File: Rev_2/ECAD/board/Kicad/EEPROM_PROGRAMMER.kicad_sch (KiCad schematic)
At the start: 4 parts, among them U1 FT232RL

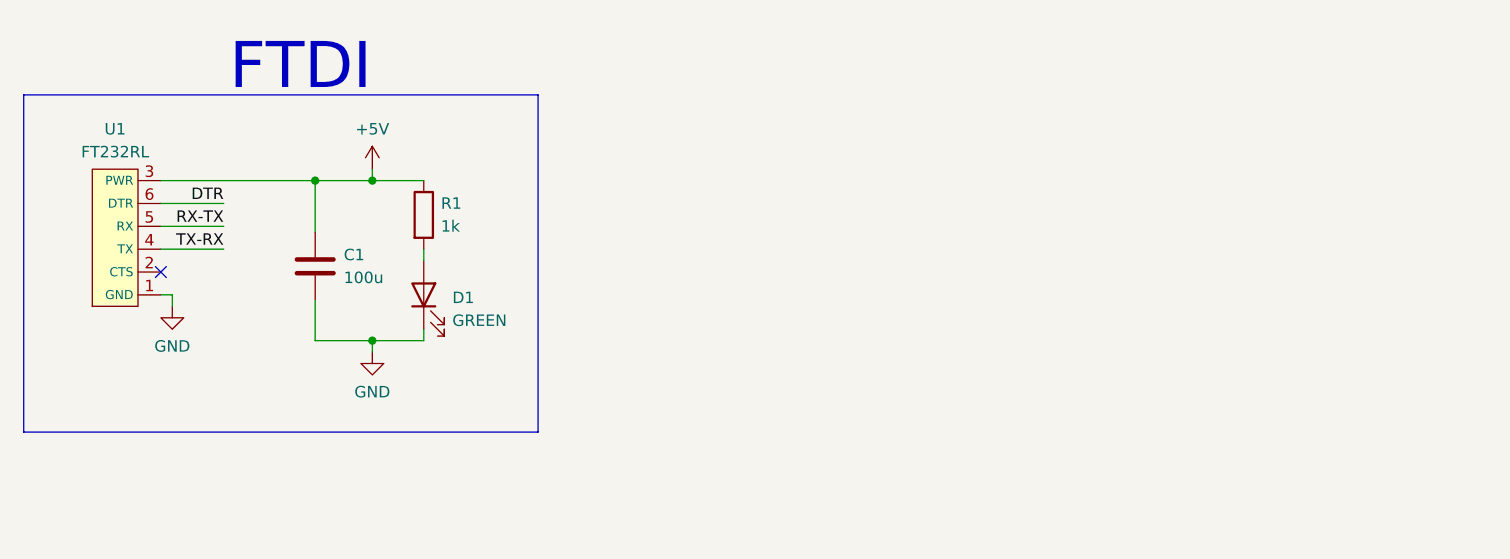
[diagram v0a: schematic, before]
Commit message: Added Reverse Polarity Protection and Overvoltage Portection
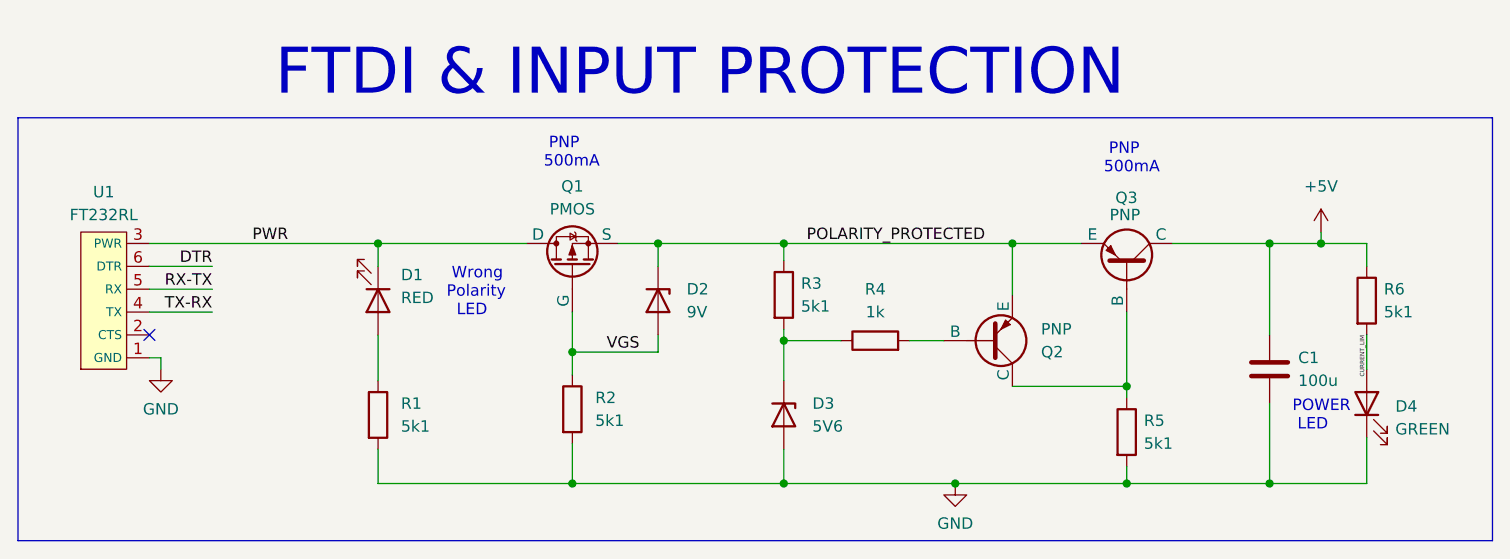
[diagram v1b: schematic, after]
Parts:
- added D1: RED, LED_SMD:LED_0805_2012Metric_Pad1.15x1.40mm_HandSolder, symbol Device:LED
- added D2: 9V, symbol Device:D_Zener
- added D3: 5V6, symbol Device:D_Zener
- added Q1: PMOS, Package_TO_SOT_SMD:SOT-23, symbol Simulation_SPICE:PMOS
- added Q2: PNP, Package_TO_SOT_SMD:SOT-23, symbol Simulation_SPICE:PNP
- added Q3: PNP, Package_TO_SOT_THT:TO-92, symbol Simulation_SPICE:PNP
- added R1, R2, R3, R5: 5k1, Resistor_SMD:R_0805_2012Metric_Pad1.20x1.40mm_HandSolder, symbol Device:R
- added R4: 1k, Resistor_SMD:R_0805_2012Metric_Pad1.20x1.40mm_HandSolder, symbol Device:R
- C1: footprint (none) -> Capacitor_THT:CP_Radial_D6.3mm_P2.50mm
- R6: renamed from R1; value 1k -> 5k1
- renumbered D1 to D4
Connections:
- net +5V: now also Q3.1 (C); no longer U1.3 (PWR)
- net GND: now also D3.2 (A), R1.2, R2.2, R5.2
- net CURRENT_LIM: now reaches D4.2 (A), R6.2
- new net: D3.1 (K), R3.2, R4.1
- new net: Q2.2 (B), R4.2
- new net: Q2.1 (C), Q3.2 (B), R5.1
- new net: D1.2 (A), R1.1
- new net POLARITY_PROTECTED: D2.1 (K), Q1.3 (S), Q2.3 (E), Q3.3 (E), R3.1
- new net PWR: D1.1 (K), Q1.1 (D), U1.3 (PWR)
- new net VGS: D2.2 (A), Q1.2 (G), R2.1
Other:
- note added: "FTDI & INPUT PROTECTION"
- note added: "PNP 500mA"
- note added: "POWER LED"
- note added: "Wrong Polarity LED"
- note removed: "FTDI"
- moved on the sheet: C1, D4, R6, U1

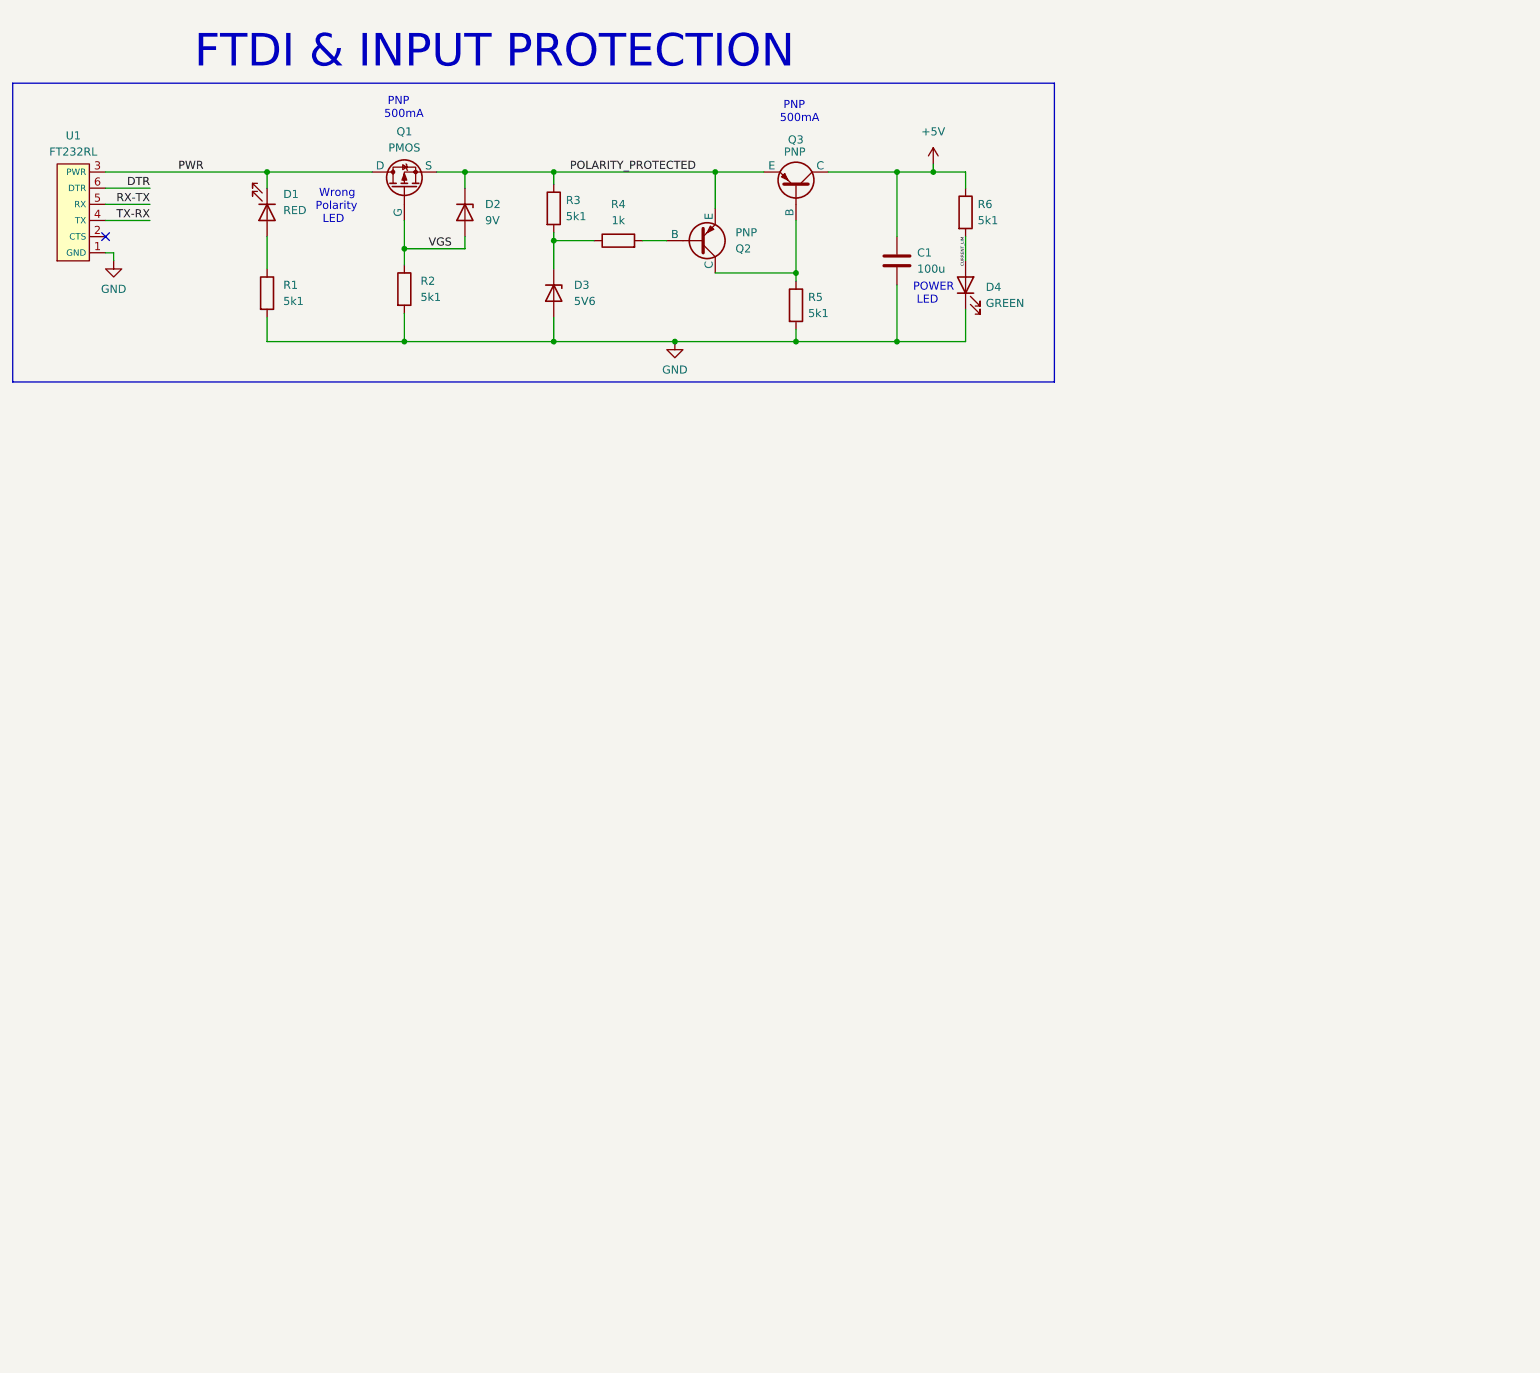
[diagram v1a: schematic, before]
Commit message: Added Atmega328 to the schematic
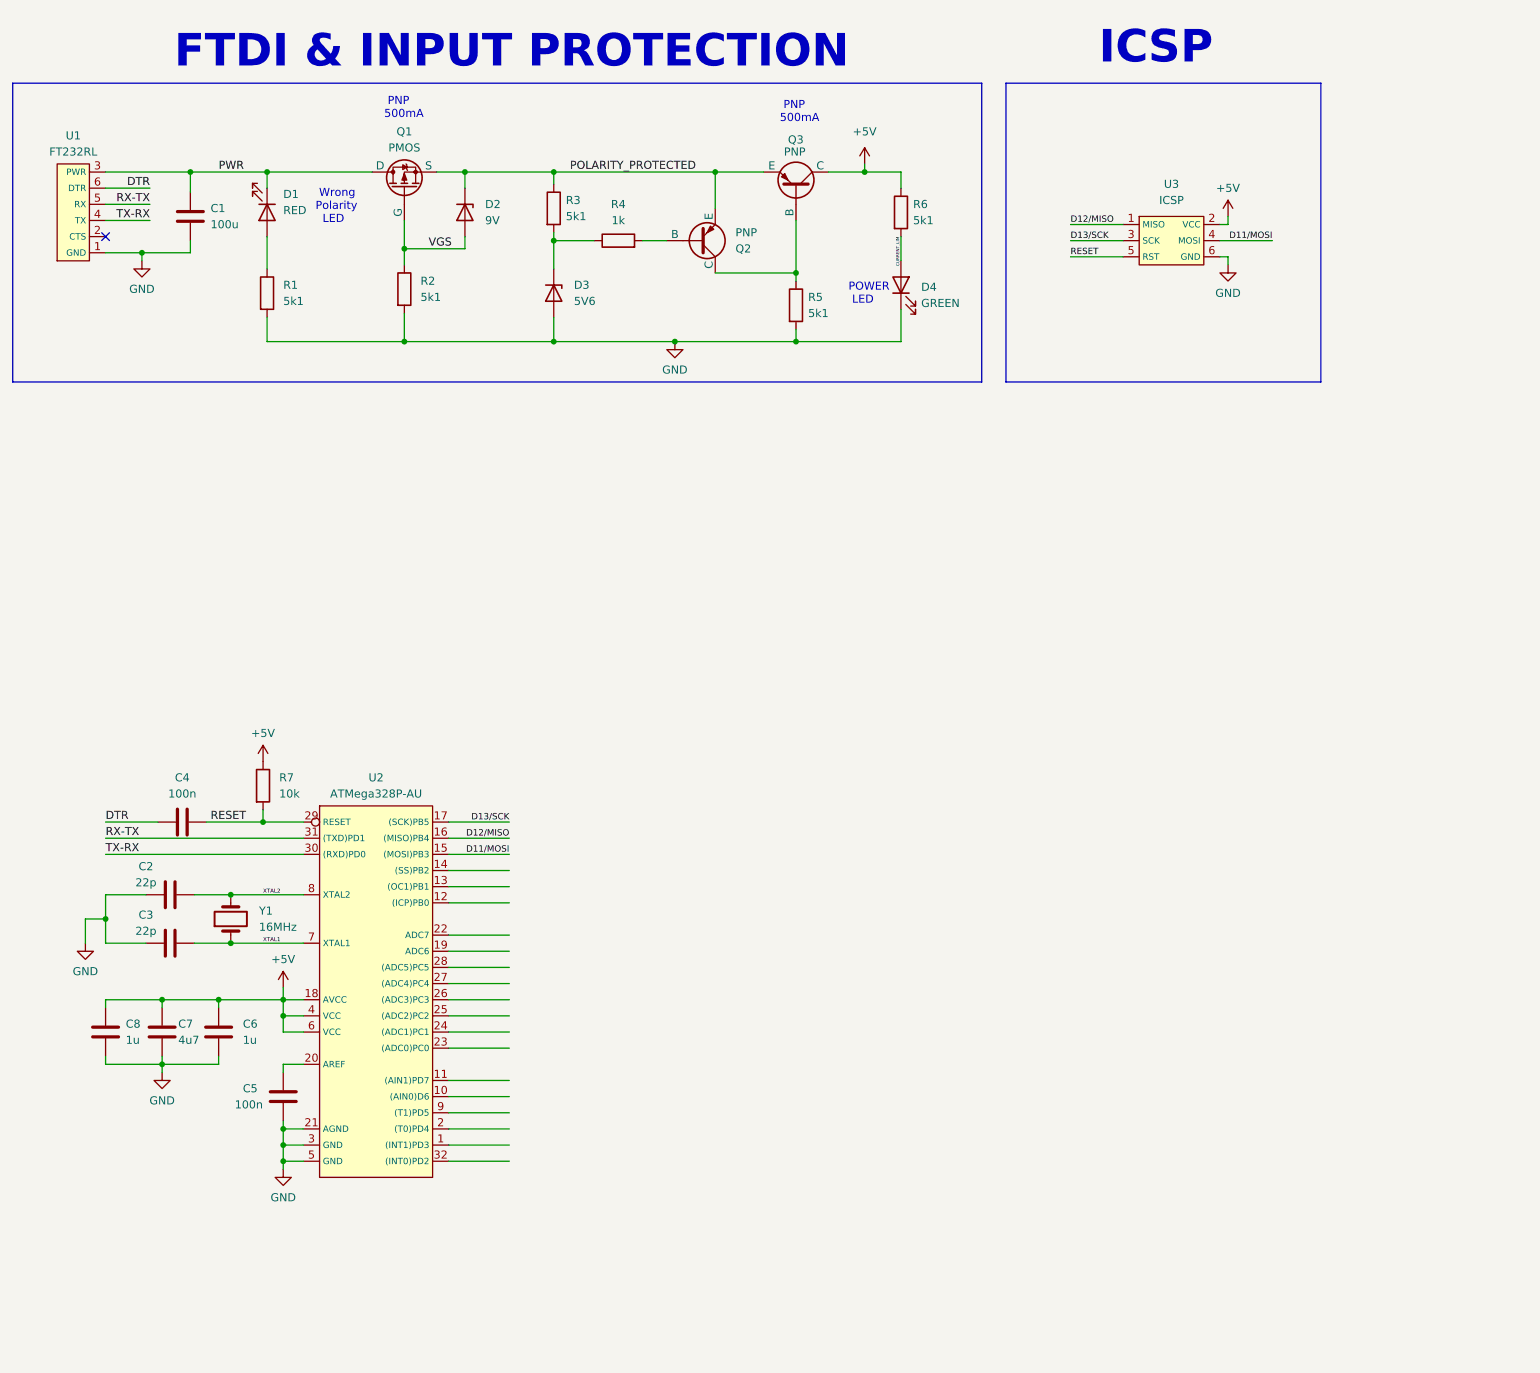
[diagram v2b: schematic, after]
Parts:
- added C2, C3: 22p, Capacitor_THT:CP_Radial_D6.3mm_P2.50mm, symbol Device:C
- added C4, C5: 100n, Capacitor_THT:CP_Radial_D6.3mm_P2.50mm, symbol Device:C
- added C6, C8: 1u, Capacitor_THT:CP_Radial_D6.3mm_P2.50mm, symbol Device:C
- added C7: 4u7, Capacitor_THT:CP_Radial_D6.3mm_P2.50mm, symbol Device:C
- added R7: 10k, Resistor_SMD:R_0805_2012Metric_Pad1.20x1.40mm_HandSolder, symbol Device:R
- added U2: ATMega328P-AU, EEPROM_PROGRAMMER:ATMega328P-AU, symbol EEPROM_PROGRAMMER:ATMega328P-AU
- added U3: ICSP, EEPROM_PROGRAMMER:ICSP, symbol EEPROM_PROGRAMMER:ICSP
- added Y1: 16MHz, symbol Device:Crystal
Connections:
- net +5V: now also C6.2, C7.2, C8.2, R7.1, U2.18 (AVCC), U2.4 (VCC), U2.6 (VCC), U3.2 (VCC); no longer C1.1
- net DTR: now also C4.1
- net GND: now also C2.1, C3.1, C5.1, C6.1, C7.1, C8.1, U2.21 (AGND), U2.3 (GND), U2.5 (GND), U3.6 (GND)
- net PWR: now also C1.1
- net RX-TX: now also U2.31 ((TXD)PD1)
- net TX-RX: now also U2.30 ((RXD)PD0)
- new net: C5.2, U2.20 (AREF)
- new net D11/MOSI: U2.15 ((MOSI)PB3), U3.4 (MOSI)
- new net D12/MISO: U2.16 ((MISO)PB4), U3.1 (MISO)
- new net D13/SCK: U2.17 ((SCK)PB5), U3.3 (SCK)
- new net RESET: C4.2, R7.2, U2.29 (RESET), U3.5 (RST)
- new net XTAL1: C3.2, U2.7 (XTAL1), Y1.1
- new net XTAL2: C2.2, U2.8 (XTAL2), Y1.2
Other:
- note added: "ICSP"
- moved on the sheet: D4, R6

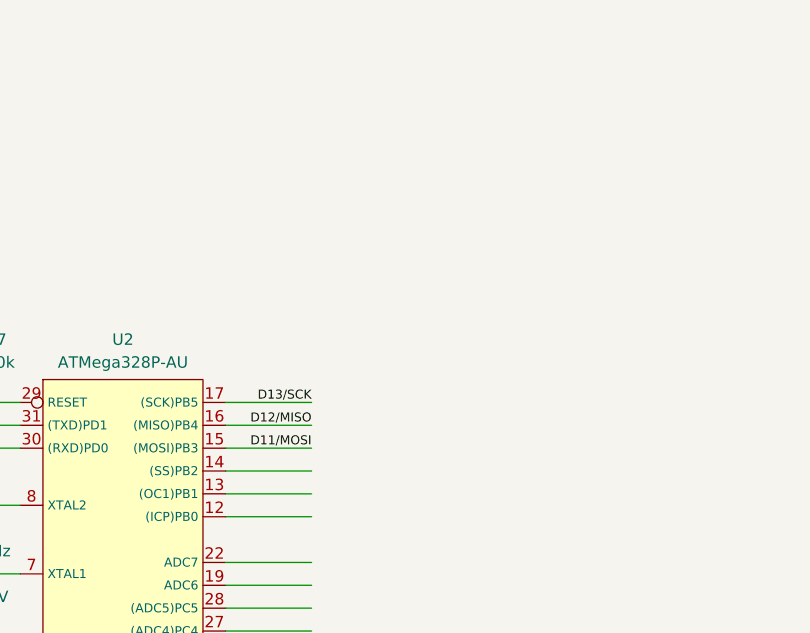
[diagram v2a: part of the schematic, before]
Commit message: Added SD-Card Reader to schematic
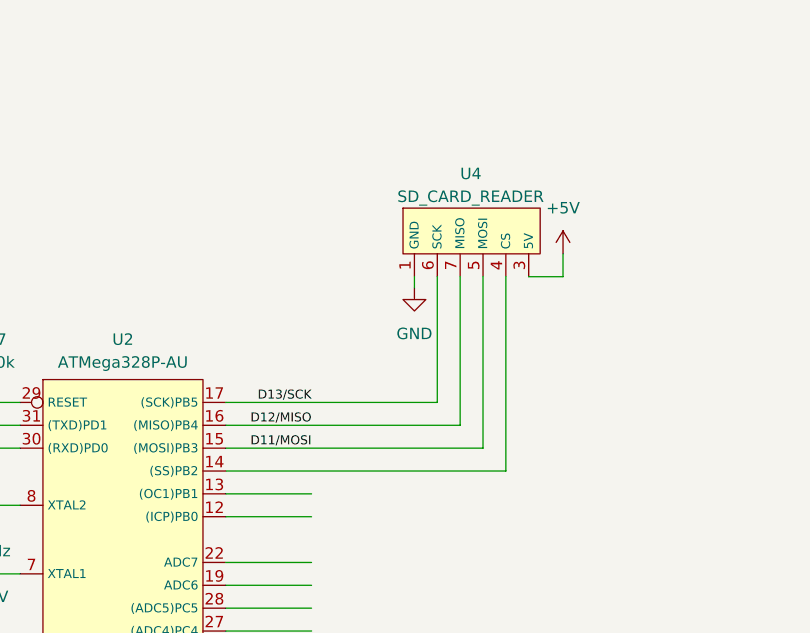
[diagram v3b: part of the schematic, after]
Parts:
- added U4: SD_CARD_READER, EEPROM_PROGRAMMER:SD_CARD_READER, symbol EEPROM_PROGRAMMER:SD_CARD_READER
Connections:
- net +5V: now also U4.3 (5V)
- net D11/MOSI: now also U4.5 (MOSI)
- net D12/MISO: now also U4.7 (MISO)
- net D13/SCK: now also U4.6 (SCK)
- net GND: now also U4.1 (GND)
- net at U2.14 ((SS)PB2): now also U4.4 (CS)
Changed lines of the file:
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@@
-    (stroke (width 0) (type default))
-  )
-  (wire (pts (xy 85.725 146.05) (xy 95.25 146.05))
     (stroke (width 0) (type default))
   )
@@
     (stroke (width 0) (type default))
   )
+  (wire (pts (xy 109.22 127) (xy 109.22 140.97))
+    (stroke (width 0) (type default))
+  )
   (wire (pts (xy 62.865 189.23) (xy 59.69 189.23))
     (stroke (width 0) (type default))
@@
     (stroke (width 0) (type default))
   )
+  (wire (pts (xy 116.84 127) (xy 116.84 148.59))
+    (stroke (width 0) (type default))
+  )
   (wire (pts (xy 140.335 65.405) (xy 156.845 65.405))
     (stroke (width 0) (type default))
@@
     (stroke (width 0) (type default))
   )
+  (wire (pts (xy 111.76 127) (xy 111.76 143.51))
+    (stroke (width 0) (type default))
+  )
   (wire (pts (xy 102.235 40.64) (xy 102.235 38.735))
     (stroke (width 0) (type default))
   )
+  (wire (pts (xy 85.725 146.05) (xy 114.3 146.05))
+    (stroke (width 0) (type default))
+  )
   (wire (pts (xy 208.28 45.72) (xy 208.28 46.99))
     (stroke (width 0) (type default))
@@
     (stroke (width 0) (type default))
   )
-  (wire (pts (xy 85.725 140.97) (xy 95.25 140.97))
+  (wire (pts (xy 85.725 140.97) (xy 109.22 140.97))
     (stroke (width 0) (type default))
   )
@@
     (stroke (width 0) (type default))
   )
-  (wire (pts (xy 85.725 143.51) (xy 95.25 143.51))
+  (wire (pts (xy 85.725 143.51) (xy 111.76 143.51))
     (stroke (width 0) (type default))
   )
@@
     (stroke (width 0) (type default))
   )
+  (wire (pts (xy 123.19 127) (xy 119.38 127))
+    (stroke (width 0) (type default))
+  )
   (wire (pts (xy 85.725 166.37) (xy 95.25 166.37))
     (stroke (width 0) (type default))
@@
     (stroke (width 0) (type default))
   )
-  (wire (pts (xy 85.725 148.59) (xy 95.25 148.59))
+  (wire (pts (xy 85.725 148.59) (xy 116.84 148.59))
     (stroke (width 0) (type default))
   )
@@
     (stroke (width 0) (type default))
   )
+  (wire (pts (xy 106.68 127) (xy 106.68 128.27))
+    (stroke (width 0) (type default))
+  )
   (wire (pts (xy 102.235 49.53) (xy 108.585 49.53))
     (stroke (width 0) (type default))
@@
     (stroke (width 0) (type default))
   )
+  (wire (pts (xy 123.19 124.46) (xy 123.19 127))
+    (stroke (width 0) (type default))
+  )
   (wire (pts (xy 121.285 65.405) (xy 102.235 65.405))
     (stroke (width 0) (type default))
   )
   (wire (pts (xy 37.465 52.705) (xy 37.465 51.435))
+    (stroke (width 0) (type default))
+  )
+  (wire (pts (xy 114.3 127) (xy 114.3 146.05))
     (stroke (width 0) (type default))
   )
@@
     )
   )
+  (symbol (lib_id "power:+5V") (at 123.19 124.46 0) (unit 1)
+    (in_bom yes) (on_board yes) (dnp no) (fields_autoplaced)
+    (property "Reference" "#PWR011" (at 123.19 128.27 0)
+      (effects (font (size 1.27 1.27)) hide)
+    )
+    (property "Value" "+5V" (at 123.19 119.38 0)
+      (effects (font (size 1.27 1.27)))
+    )
+    (property "Footprint" "" (at 123.19 124.46 0)
+      (effects (font (size 1.27 1.27)) hide)
+    )
+    (property "Datasheet" "" (at 123.19 124.46 0)
+      (effects (font (size 1.27 1.27)) hide)
+    )
+    (pin "1")
+    (instances
+      (project "EEPROM_PROGRAMMER"
+        (path "/bc7d165f-daf1-4bac-b7f4-5fbe134c87cf"
+          (reference "#PWR011") (unit 1)
+        )
+      )
+    )
+  )
   (symbol (lib_id "Simulation_SPICE:PNP") (at 140.335 41.275 270) (mirror x) (unit 1)
     (in_bom yes) (on_board yes) (dnp no)
@@
         (path "/bc7d165f-daf1-4bac-b7f4-5fbe134c87cf"
           (reference "Q3") (unit 1)
+        )
+      )
+    )
+  )
+  (symbol (lib_id "power:GND") (at 106.68 128.27 0) (unit 1)
+    (in_bom yes) (on_board yes) (dnp no) (fields_autoplaced)
+    (property "Reference" "#PWR012" (at 106.68 134.62 0)
+      (effects (font (size 1.27 1.27)) hide)
+    )
+    (property "Value" "GND" (at 106.68 133.35 0)
+      (effects (font (size 1.27 1.27)))
+    )
+    (property "Footprint" "" (at 106.68 128.27 0)
+      (effects (font (size 1.27 1.27)) hide)
+    )
+    (property "Datasheet" "" (at 106.68 128.27 0)
+      (effects (font (size 1.27 1.27)) hide)
+    )
+    (pin "1")
+    (instances
+      (project "EEPROM_PROGRAMMER"
+        (path "/bc7d165f-daf1-4bac-b7f4-5fbe134c87cf"
+          (reference "#PWR012") (unit 1)
         )
       )
@@
         )
       )
+    )
+  )
+  (symbol (lib_id "EEPROM_PROGRAMMER:SD_CARD_READER") (at 113.03 121.92 0) (unit 1)
+    (in_bom yes) (on_board yes) (dnp no)
+    (property "Reference" "U4" (at 111.76 115.57 0)
+      (effects (font (size 1.27 1.27)) (justify left))
+    )
+    (property "Value" "SD_CARD_READER" (at 104.775 118.11 0)
+      (effects (font (size 1.27 1.27)) (justify left))
+    )
+    (property "Footprint" "EEPROM_PROGRAMMER:SD_CARD_READER" (at 115.57 109.22 0)
+      (effects (font (size 1.27 1.27)) hide)
+    )
+    (property "Datasheet" "https://www.electrokit.com/upload/product/41015/41015739/41015739_-_SD_Card_Module.pdf" (at 114.3 111.76 0)
+      (effects (font (size 1.27 1.27)) hide)
+    )
+    (pin "1")
+    (pin "3")
+    (pin "4")
+    (pin "5")
+    (pin "6")
+    (pin "7")
+    (instances
+      (project "EEPROM_PROGRAMMER"
+        (path "/bc7d165f-daf1-4bac-b7f4-5fbe134c87cf"
+          (reference "U4") (unit 1)
+        )
+      )
